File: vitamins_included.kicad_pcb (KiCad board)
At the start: 2 copper layers, 230.5 x 82 mm, 136 parts, among them J1 Speaker, J10 UTC16-G, J2 reset, J3 ISP, J4 reset, J5 Speaker, J6 ISP, J7 Sig, J8 Sig, J9 UTC16-G, P3 WS2812, P4 SJ-43514-SMT, P6 WS2812, P8 SJ-43514-SMT, SW1 Socket, SW10 Socket, SW11 Socket, SW12 Socket, SW13 Socket, SW14 Socket, SW15 Socket, SW16 Socket, SW17 Socket, SW18 Socket, SW19 Socket, SW2 Socket, SW20 Socket, SW21 Socket, SW22 Socket, SW23 Socket, SW24 Socket, SW25 Socket, SW26 Socket, SW27 Socket, SW28 Socket, SW29 Socket, SW3 Socket, SW30 Socket, SW31 Socket, SW32 Socket, SW33 Socket, SW34 Socket, SW35 Socket, SW36 Socket, SW37 Socket, SW38 Socket, SW39 Socket, SW4 Socket, SW40 Socket, SW41 Socket, SW42 Socket, SW43 Socket, SW44 Socket, SW45 Socket, SW46 Socket, SW47 Socket, SW48 Socket, SW5 Socket, SW6 Socket, SW7 Socket, SW8 Socket, SW9 Socket, U1 ATMega32U4, U2 ATMega32U4, Y1 16MHz, Y2 16MHz

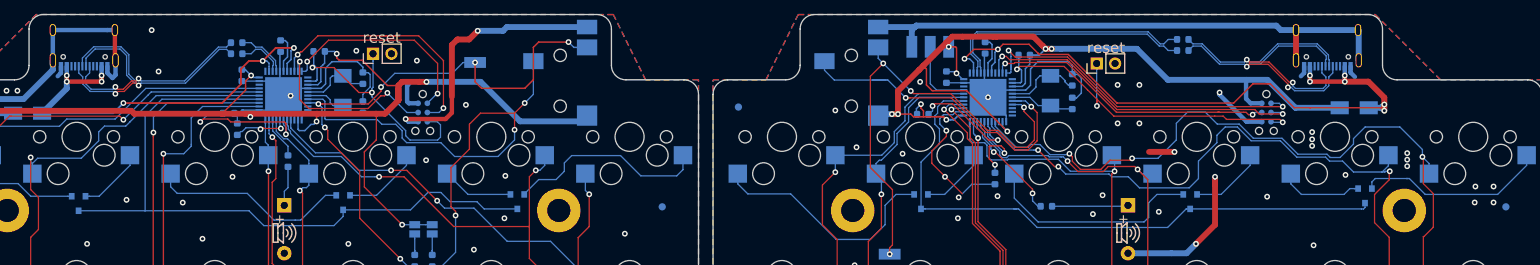
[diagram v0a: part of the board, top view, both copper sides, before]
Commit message: Organized silkscreen
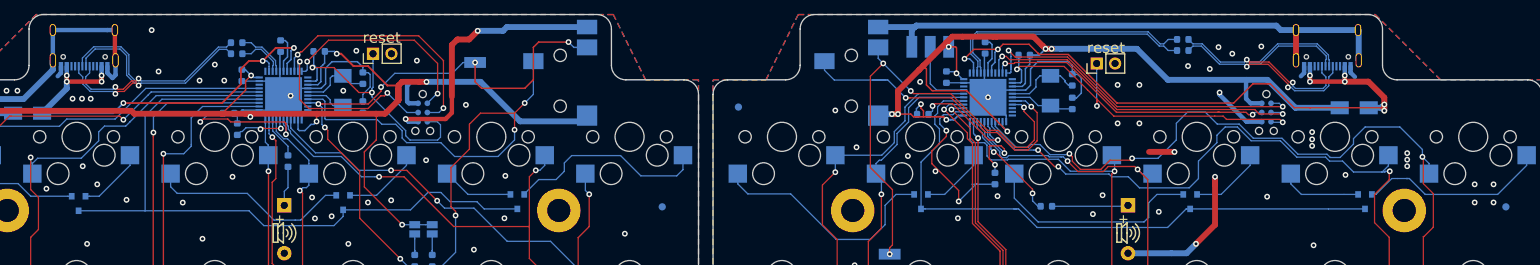
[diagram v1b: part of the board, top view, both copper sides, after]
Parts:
- moved D15 0.80 mm to (206.1, 25.8)
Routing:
- net GND: track 302.9 -> 305.4 mm, vias 88 -> 109
- net /Right half/row0: track 83.8 -> 83.1 mm
- net (no net): vias 1 -> 0

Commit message: Added reset button, led, 3D models
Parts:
- added D27: red, LED_SMD:LED_0603_1608Metric_Castellated, B.Cu at (82.2, 14.7)
- added D28: red, LED_SMD:LED_0603_1608Metric_Castellated, B.Cu at (171.4, 15.1)
- added R15: 220R, Resistor_SMD:R_0603_1608Metric, B.Cu at (77.0, 19.4)
- added R16: 220R, Resistor_SMD:R_0603_1608Metric, B.Cu at (174.8, 15.1)
- added SW49: FSMSM, Button_Switch_SMD:SW_SPST_FSMSM, B.Cu at (85.7, 11.7)
- added SW50: FSMSM, Button_Switch_SMD:SW_SPST_FSMSM, B.Cu at (176.2, 11.7)
- moved R4 1.16 mm to (51.6, 4.80)
- moved R5 1.15 mm to (51.6, 3.30)
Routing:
- net Net-(D27-Pad2): track 0.00 -> 32.0 mm, vias 0 -> 2
- net GND: track 305.4 -> 327.6 mm, vias 109 -> 108
- net Net-(D28-Pad2): track 0.00 -> 13.6 mm
- net /Right half/Dd+: track 40.0 -> 32.6 mm
- net Net-(D27-Pad1): track 0.00 -> 6.73 mm, vias 0 -> 2
- net /Right half/Dd-: track 40.0 -> 34.1 mm
- net /Left half/~Reset: track 37.7 -> 42.2 mm
- net /Left half/SCL/D3: track 76.5 -> 72.1 mm
- net /Left half/Dd+: track 39.4 -> 35.0 mm
- net /Left half/Dd-: track 39.3 -> 35.5 mm
- net VBUS: track 155.0 -> 158.7 mm
- net /Right half/~RESET: track 54.2 -> 57.2 mm
- net Net-(D28-Pad1): track 0.00 -> 1.76 mm
- net VCC: track 303.1 -> 301.8 mm
- net Net-(D3-Pad2): track 28.3 -> 27.5 mm
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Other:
- board text added: "RESET"

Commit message: Broke something. who knows
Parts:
- moved C2 0.60 mm to (68.0, 12.2)
- moved C3 0.13 mm to (68.0, 8.90), turned to 270 degrees
- turned C7 to 270 degrees
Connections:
- J10 pad A5: Net-(J10-PadA5) -> (no net)
- J10 pad A8: Net-(J10-PadA8) -> (no net)
- J10 pad B5: Net-(J10-PadB5) -> (no net)
- J10 pad B8: Net-(J10-PadB8) -> (no net)
- J9 pad A5: Net-(J9-PadA5) -> (no net)
- J9 pad A8: Net-(J9-PadA8) -> (no net)
- J9 pad B5: Net-(J9-PadB5) -> (no net)
- J9 pad B8: Net-(J9-PadB8) -> (no net)
- U1 pad 1: Net-(U1-Pad1) -> (no net)
- U1 pad 12: Net-(U1-Pad12) -> (no net)
- U1 pad 20: Net-(U1-Pad20) -> (no net)
- U1 pad 21: Net-(U1-Pad21) -> (no net)
- U1 pad 25: Net-(U1-Pad25) -> (no net)
- U1 pad 42: Net-(U1-Pad42) -> (no net)
- U1 pad 8: Net-(U1-Pad8) -> (no net)
- U2 pad 1: Net-(U2-Pad1) -> (no net)
- U2 pad 12: Net-(U2-Pad12) -> (no net)
- U2 pad 20: Net-(U2-Pad20) -> (no net)
- U2 pad 21: Net-(U2-Pad21) -> (no net)
- U2 pad 25: Net-(U2-Pad25) -> (no net)
- U2 pad 42: Net-(U2-Pad42) -> (no net)
- U2 pad 8: Net-(U2-Pad8) -> (no net)
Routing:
- net GND: track 327.6 -> 340.1 mm, vias 108 -> 124
- net /Left half/MOSI: track 25.5 -> 34.8 mm
- net /Right half/col1: track 77.6 -> 86.8 mm
- net /Left half/col5: track 130.0 -> 137.7 mm
- net /Left half/SDA: track 78.6 -> 73.3 mm
- net /Left half/~Reset: track 42.2 -> 46.4 mm
- net /Right half/col5: track 141.6 -> 144.1 mm
- net /Left half/col4: track 110.8 -> 113.0 mm
- net /Right half/col0: track 99.9 -> 102.0 mm
- net /Left half/col1: track 105.9 -> 107.3 mm
- net Net-(D14-Pad1): track 30.3 -> 31.7 mm
- net /Left half/SCL/D3: track 72.1 -> 73.2 mm
- net /Left half/col0: track 118.6 -> 119.7 mm
- net /Right half/buzz: track 15.8 -> 16.7 mm
- net /Right half/col4: track 135.4 -> 136.2 mm
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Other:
- rule pad_to_mask_clearance: 0.2 -> 0.1

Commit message: Delfi
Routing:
- net /Left half/col1: track 107.3 -> 104.3 mm
- net Net-(D7-Pad1): track 36.7 -> 34.8 mm
- net Net-(D13-Pad1): track 33.0 -> 33.8 mm
- net GND: vias 124 -> 129

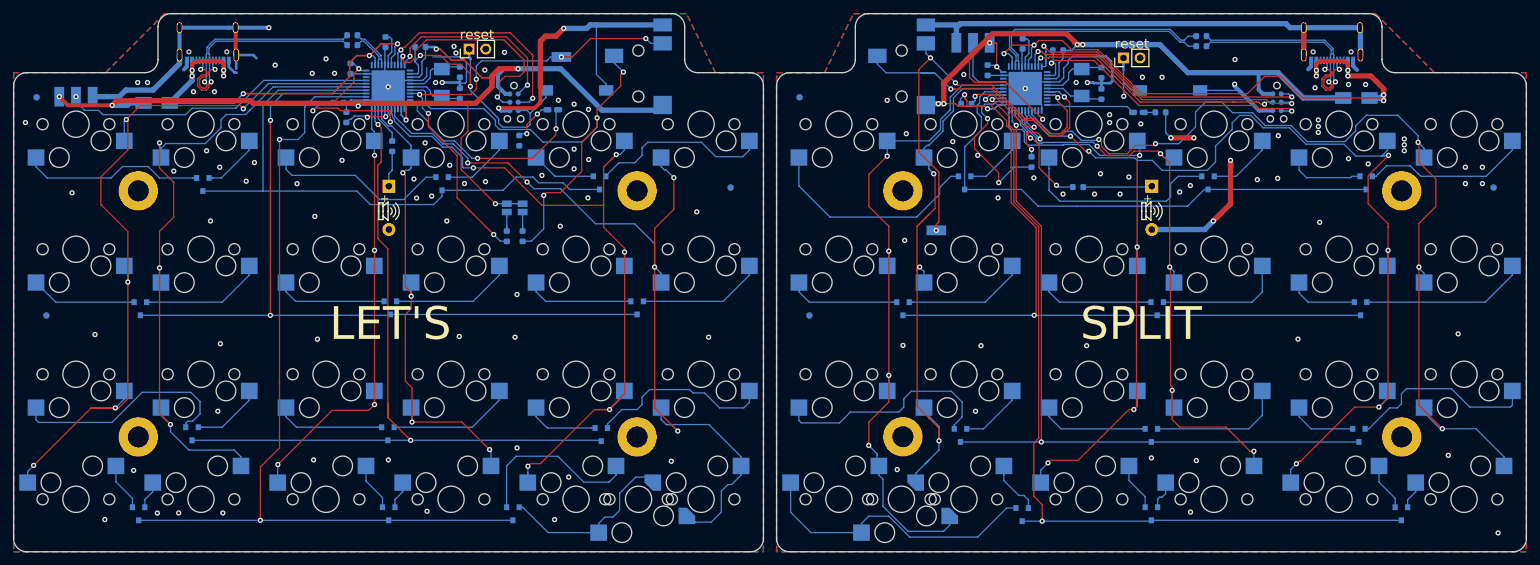
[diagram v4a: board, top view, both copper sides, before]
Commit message: Added WS2812B leds to one half
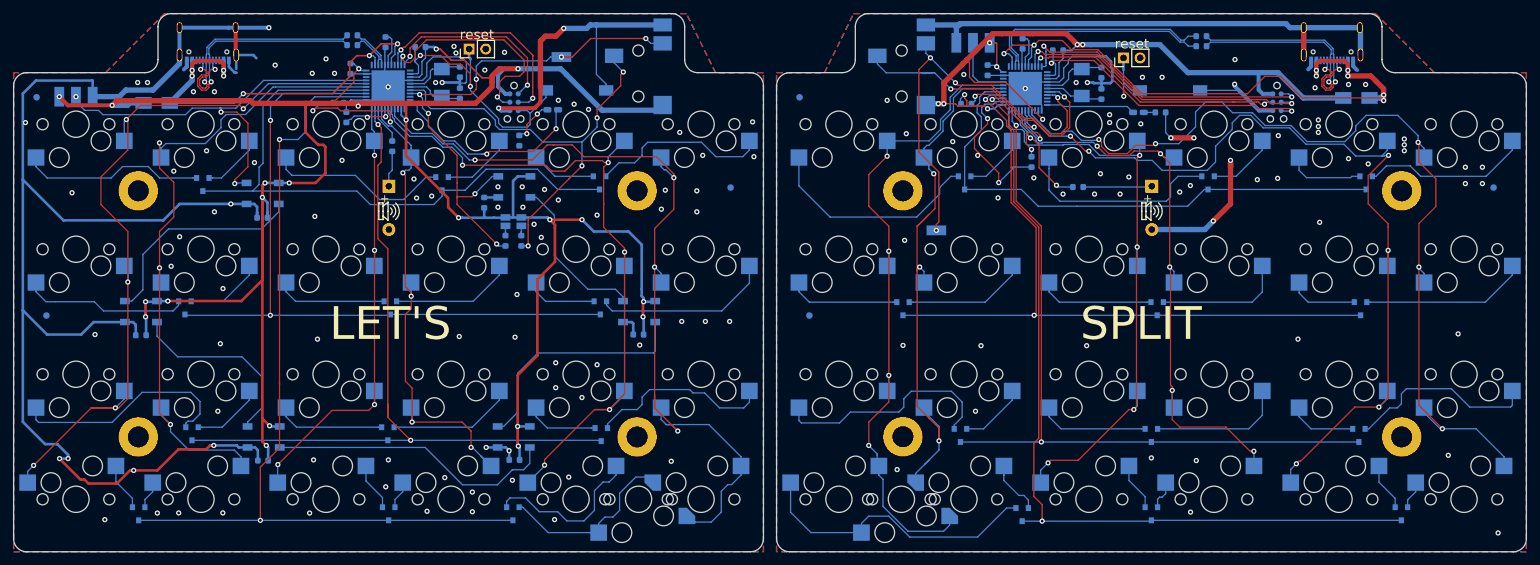
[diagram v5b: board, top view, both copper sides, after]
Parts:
- added C10: 1uF, Capacitor_SMD:C_0603_1608Metric, B.Cu at (19.4, 49.0)
- added C11: 1uF, Capacitor_SMD:C_0603_1608Metric, B.Cu at (38.0, 68.1)
- added C12: 1uF, Capacitor_SMD:C_0603_1608Metric, B.Cu at (76.3, 68.0)
- added C13: 1uF, Capacitor_SMD:C_0603_1608Metric, B.Cu at (95.2, 48.9)
- added C14: 1uF, Capacitor_SMD:C_0603_1608Metric, B.Cu at (71.7, 28.8)
- added C9: 1uF, Capacitor_SMD:C_0603_1608Metric, B.Cu at (37.9, 31.1)
- added D29: WS2812B, LED_SMD:LED_WS2812B_PLCC4_5.0x5.0mm_P3.2mm, B.Cu at (38.0, 27.4)
- added D30: WS2812B, LED_SMD:LED_WS2812B_PLCC4_5.0x5.0mm_P3.2mm, B.Cu at (19.4, 45.4)
- added D31: WS2812B, LED_SMD:LED_WS2812B_PLCC4_5.0x5.0mm_P3.2mm, B.Cu at (38.1, 64.5)
- added D32: WS2812B, LED_SMD:LED_WS2812B_PLCC4_5.0x5.0mm_P3.2mm, B.Cu at (76.3, 26.4)
- added D33: WS2812B, LED_SMD:LED_WS2812B_PLCC4_5.0x5.0mm_P3.2mm, B.Cu at (95.3, 45.4)
- added D34: WS2812B, LED_SMD:LED_WS2812B_PLCC4_5.0x5.0mm_P3.2mm, B.Cu at (76.2, 64.5)
- moved D4 6.79 mm to (26.1, 44.8)
- moved D6 5.60 mm to (89.4, 44.8)
- moved JP1 2.11 mm to (74.9, 31.7)
- moved JP2 2.11 mm to (77.4, 31.7)
- moved R1 0.73 mm to (74.9, 34.6)
- moved R2 0.73 mm to (77.4, 34.6)
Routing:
- net VCC: track 301.8 -> 505.7 mm, vias 17 -> 31
- net GND: track 340.1 -> 526.5 mm, vias 129 -> 151
- net Net-(D31-Pad2): track 0.00 -> 44.3 mm
- net Net-(D33-Pad2): track 0.00 -> 36.7 mm
- net Net-(D29-Pad2): track 0.00 -> 33.4 mm
- net Net-(D30-Pad2): track 0.00 -> 29.1 mm
- net Net-(D32-Pad2): track 0.00 -> 25.0 mm
- net /Left half/wd2812-in: track 48.0 -> 65.4 mm, vias 1 -> 3
- net /Left half/row1: track 123.0 -> 110.7 mm
- net Net-(D4-Pad1): track 16.2 -> 25.3 mm
- net /Left half/SDA: track 73.7 -> 82.1 mm, vias 6 -> 7
- net Net-(D6-Pad2): track 19.2 -> 27.1 mm
- net Net-(D4-Pad2): track 18.8 -> 11.9 mm
- net Net-(D6-Pad1): track 16.4 -> 10.8 mm
- net /Left half/SCL/D3: track 72.8 -> 68.0 mm, vias 3 -> 4
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
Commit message: started work on second half
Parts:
- added C15: 1uF, Capacitor_SMD:C_0603_1608Metric, B.Cu at (154.1, 31.1)
- added C16: 1uF, Capacitor_SMD:C_0603_1608Metric, B.Cu at (135.7, 49.0)
- added C17: 1uF, Capacitor_SMD:C_0603_1608Metric, B.Cu at (154.2, 68.1)
- added C18: 1uF, Capacitor_SMD:C_0603_1608Metric, B.Cu at (192.7, 22.9)
- added C19: 1uF, Capacitor_SMD:C_0603_1608Metric, B.Cu at (211.4, 48.9)
- added C20: 1uF, Capacitor_SMD:C_0603_1608Metric, B.Cu at (192.6, 68.0)
- added D35: WS2812B, LED_SMD:LED_WS2812B_PLCC4_5.0x5.0mm_P3.2mm, B.Cu at (154.2, 27.4)
- added D36: WS2812B, LED_SMD:LED_WS2812B_PLCC4_5.0x5.0mm_P3.2mm, B.Cu at (135.7, 45.4)
- added D37: WS2812B, LED_SMD:LED_WS2812B_PLCC4_5.0x5.0mm_P3.2mm, B.Cu at (154.3, 64.5)
- added D38: WS2812B, LED_SMD:LED_WS2812B_PLCC4_5.0x5.0mm_P3.2mm, B.Cu at (192.6, 26.4)
- added D39: WS2812B, LED_SMD:LED_WS2812B_PLCC4_5.0x5.0mm_P3.2mm, B.Cu at (211.6, 45.4)
- added D40: WS2812B, LED_SMD:LED_WS2812B_PLCC4_5.0x5.0mm_P3.2mm, B.Cu at (192.4, 64.5)
- moved J8 24.0 mm to (127.8, 12.7)
- moved D16 6.59 mm to (142.1, 45.0)
- moved G*** 0.60 mm to (193.5, 31.4)
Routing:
- net Net-(D35-Pad2): track 0.00 -> 34.1 mm
- net /Right half/WD2812-in: track 10.1 -> 35.5 mm, vias 0 -> 2
- net /Right half/SDA: track 63.8 -> 50.1 mm, vias 4 -> 5
- net Net-(D16-Pad1): track 17.0 -> 24.3 mm
- net VCC: track 505.7 -> 512.4 mm
- net Net-(D16-Pad2): track 18.8 -> 12.2 mm
- net /Right half/row1: track 108.9 -> 102.3 mm
- net /Right half/row0: track 82.8 -> 86.9 mm
- net Net-(D20-Pad2): track 20.5 -> 19.2 mm
- net Net-(D18-Pad2): track 25.3 -> 26.6 mm
- net Net-(D14-Pad1): track 31.7 -> 30.9 mm
- net /Right half/col3: track 91.9 -> 91.1 mm
- net GND: track 526.5 -> 526.6 mm, vias 151 -> 147

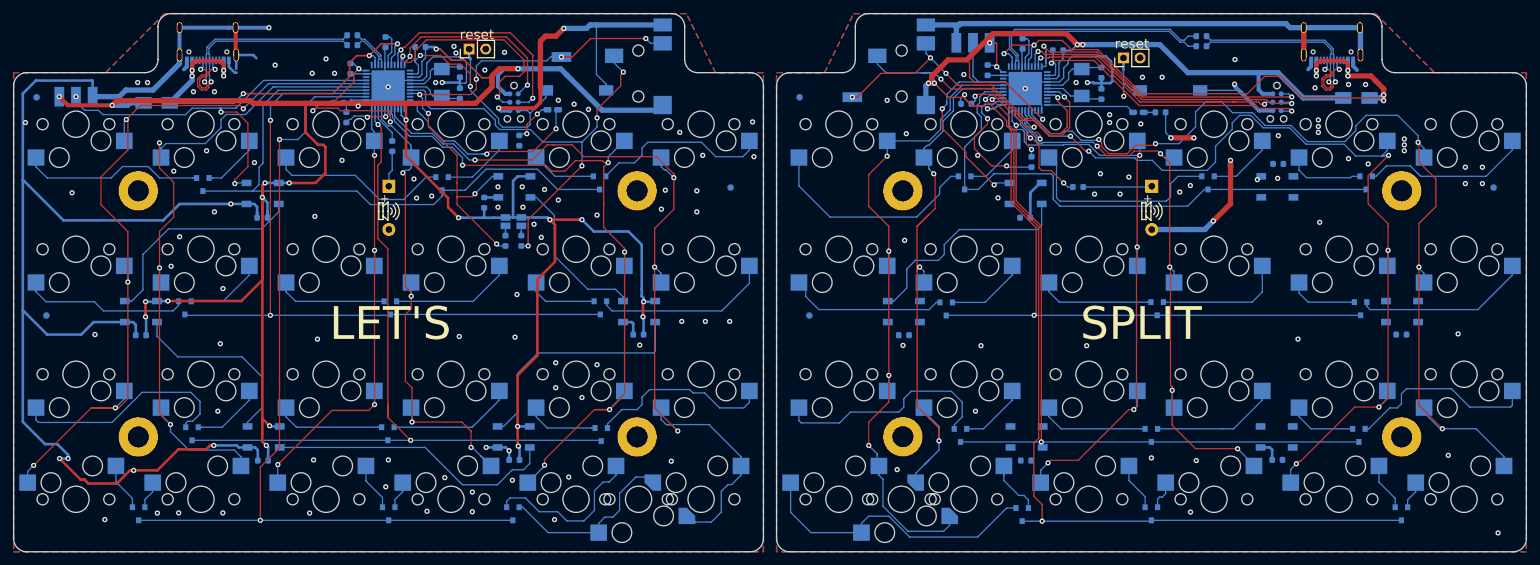
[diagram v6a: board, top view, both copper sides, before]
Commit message: Added ws2812 LEDs
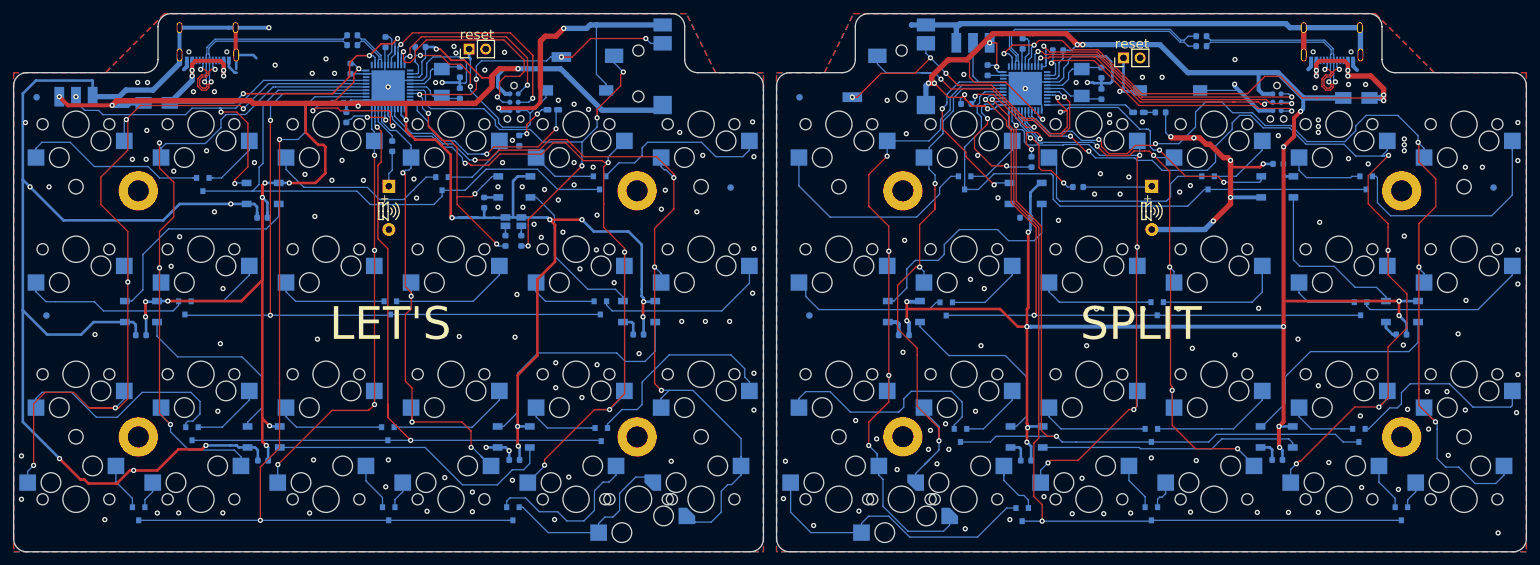
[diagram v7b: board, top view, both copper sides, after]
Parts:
- added REF**: MountingHole_2.2mm_M2, MountingHole:MountingHole_2.2mm_M2, F.Cu at (221.0, 64.5)
- added REF**: MountingHole_2.2mm_M2, MountingHole:MountingHole_2.2mm_M2, F.Cu at (125.8, 26.4)
- added REF**: MountingHole_2.2mm_M2, MountingHole:MountingHole_2.2mm_M2, F.Cu at (125.8, 64.5)
- added REF**: MountingHole_2.2mm_M2, MountingHole:MountingHole_2.2mm_M2, F.Cu at (221.0, 26.4)
- added REF**: MountingHole_2.2mm_M2, MountingHole:MountingHole_2.2mm_M2, F.Cu at (104.8, 64.5)
- added REF**: MountingHole_2.2mm_M2, MountingHole:MountingHole_2.2mm_M2, F.Cu at (9.50, 26.4)
- added REF**: MountingHole_2.2mm_M2, MountingHole:MountingHole_2.2mm_M2, F.Cu at (104.8, 26.4)
- added REF**: MountingHole_2.2mm_M2, MountingHole:MountingHole_2.2mm_M2, F.Cu at (9.50, 64.5)
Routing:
- net VCC: track 512.4 -> 757.0 mm, vias 31 -> 44
- net Net-(D37-Pad2): track 0.00 -> 39.8 mm
- net /Right half/SDA: track 50.1 -> 89.0 mm, vias 5 -> 7
- net Net-(D39-Pad2): track 0.00 -> 34.8 mm
- net GND: track 526.6 -> 556.0 mm, vias 147 -> 214
- net Net-(D36-Pad2): track 0.00 -> 29.3 mm
- net Net-(D38-Pad2): track 0.00 -> 26.6 mm
- net Net-(D15-Pad2): track 25.7 -> 37.0 mm
- net /Left half/col0: track 119.7 -> 127.4 mm
- net /Left half/SDA: track 82.1 -> 87.1 mm
- net /Left half/col5: track 134.8 -> 130.2 mm
- net Net-(D9-Pad2): track 28.3 -> 32.4 mm
- net /Right half/col5: track 144.1 -> 147.9 mm
- net /Right half/row2: track 113.1 -> 115.7 mm
- net /Right half/col4: track 136.2 -> 138.7 mm
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
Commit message: Fixed rotated LEDs, added config jumpers
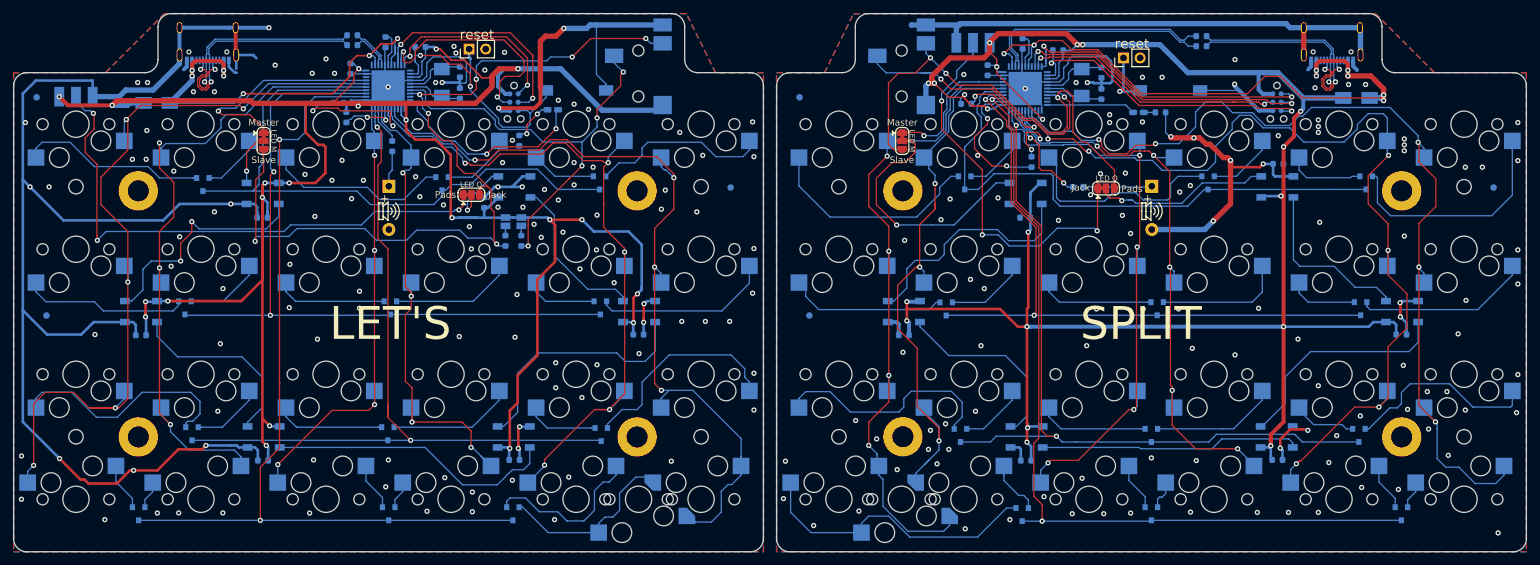
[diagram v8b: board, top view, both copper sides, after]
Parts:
- removed J7, J8: Sig, Pin_Headers:Pin_Header_Straight_1x01_Pitch2.54mm
- added JP3: WS_MODE, Jumper:SolderJumper-3_P1.3mm_Bridged12_RoundedPad1.0x1.5mm, F.Cu at (135.4, 19.4)
- added JP4: WS_MODE, Jumper:SolderJumper-3_P1.3mm_Bridged12_RoundedPad1.0x1.5mm, F.Cu at (38.1, 19.4)
- added JP5: WS_OUT, Jumper:SolderJumper-3_P1.3mm_Bridged12_RoundedPad1.0x1.5mm, F.Cu at (69.8, 27.6)
- added JP6: WS_OUT, Jumper:SolderJumper-3_P1.3mm_Bridged12_RoundedPad1.0x1.5mm, F.Cu at (166.4, 26.6)
- J5: value Speaker -> Buzzer
- turned C12 to 0 degrees
- turned C13 to 0 degrees
- turned C19 to 0 degrees
- turned C20 to 0 degrees
- turned D32 to 0 degrees
- turned D33 to 0 degrees
- turned D34 to 0 degrees
- turned D38 to 0 degrees
- turned D39 to 0 degrees
- turned D40 to 0 degrees
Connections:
- D29 pad 4: /Left half/wd2812-in -> Net-(D29-Pad4)
- D32 pad 4: /Left half/SDA -> Net-(D32-Pad4)
- D33 pad 2: Net-(D33-Pad2) -> Net-(D32-Pad4)
- D33 pad 4: Net-(D32-Pad2) -> Net-(D33-Pad4)
- D34 pad 2: Net-(D31-Pad2) -> Net-(D33-Pad4)
- D34 pad 4: Net-(D33-Pad2) -> Net-(D31-Pad2)
- D35 pad 4: /Right half/WD2812-in -> Net-(D35-Pad4)
- D38 pad 4: /Right half/SDA -> Net-(D38-Pad4)
- D39 pad 2: Net-(D39-Pad2) -> Net-(D38-Pad4)
- D39 pad 4: Net-(D38-Pad2) -> Net-(D39-Pad4)
- D40 pad 2: Net-(D37-Pad2) -> Net-(D39-Pad4)
- D40 pad 4: Net-(D39-Pad2) -> Net-(D37-Pad2)
- P3 pad 2: /Left half/wd2812-in -> /Left half/WS2812-out
- P6 pad 2: /Right half/WD2812-in -> /Right half/WD2812-out
- U1 pad 41: /Left half/wd2812-in -> /Left half/WS2812-in
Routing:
- net /Left half/WS2812-out: track 0.00 -> 84.7 mm, vias 0 -> 3
- net /Left half/wd2812-in: track 65.4 -> 0.00 mm, vias 3 -> 0
- net /Right half/WD2812-out: track 0.00 -> 59.8 mm, vias 0 -> 3
- net /Left half/SDA: track 87.1 -> 133.0 mm
- net Net-(D35-Pad4): track 0.00 -> 39.2 mm, vias 0 -> 1
- net Net-(D33-Pad4): track 0.00 -> 37.8 mm
- net Net-(D33-Pad2): track 37.8 -> 0.00 mm
- net Net-(D39-Pad4): track 0.00 -> 34.8 mm
- net Net-(D39-Pad2): track 34.8 -> 0.00 mm
- net /Left half/WS2812-in: track 0.00 -> 33.1 mm, vias 0 -> 1
- net Net-(D38-Pad4): track 0.00 -> 26.6 mm
- net Net-(D32-Pad4): track 0.00 -> 25.0 mm
- net GND: track 556.0 -> 578.1 mm, vias 214 -> 226
- net VCC: track 757.0 -> 738.8 mm, vias 44 -> 41
- net /Right half/WD2812-in: track 35.5 -> 21.8 mm, vias 2 -> 1
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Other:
- board text added: "+ D -"
- board text added: "Jack"
- board text added: "LED M"
- board text added: "LED O"
- board text added: "Master"
- board text added: "Pads"
- board text added: "Slave"
